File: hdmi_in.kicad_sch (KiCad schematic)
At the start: 46 parts, among them J3 HDMI_A, U1 M24C64-RMN6TP, U2 MS2109, U7 MT3520B, U8 MT3520B, Y1 24MHz 12pF

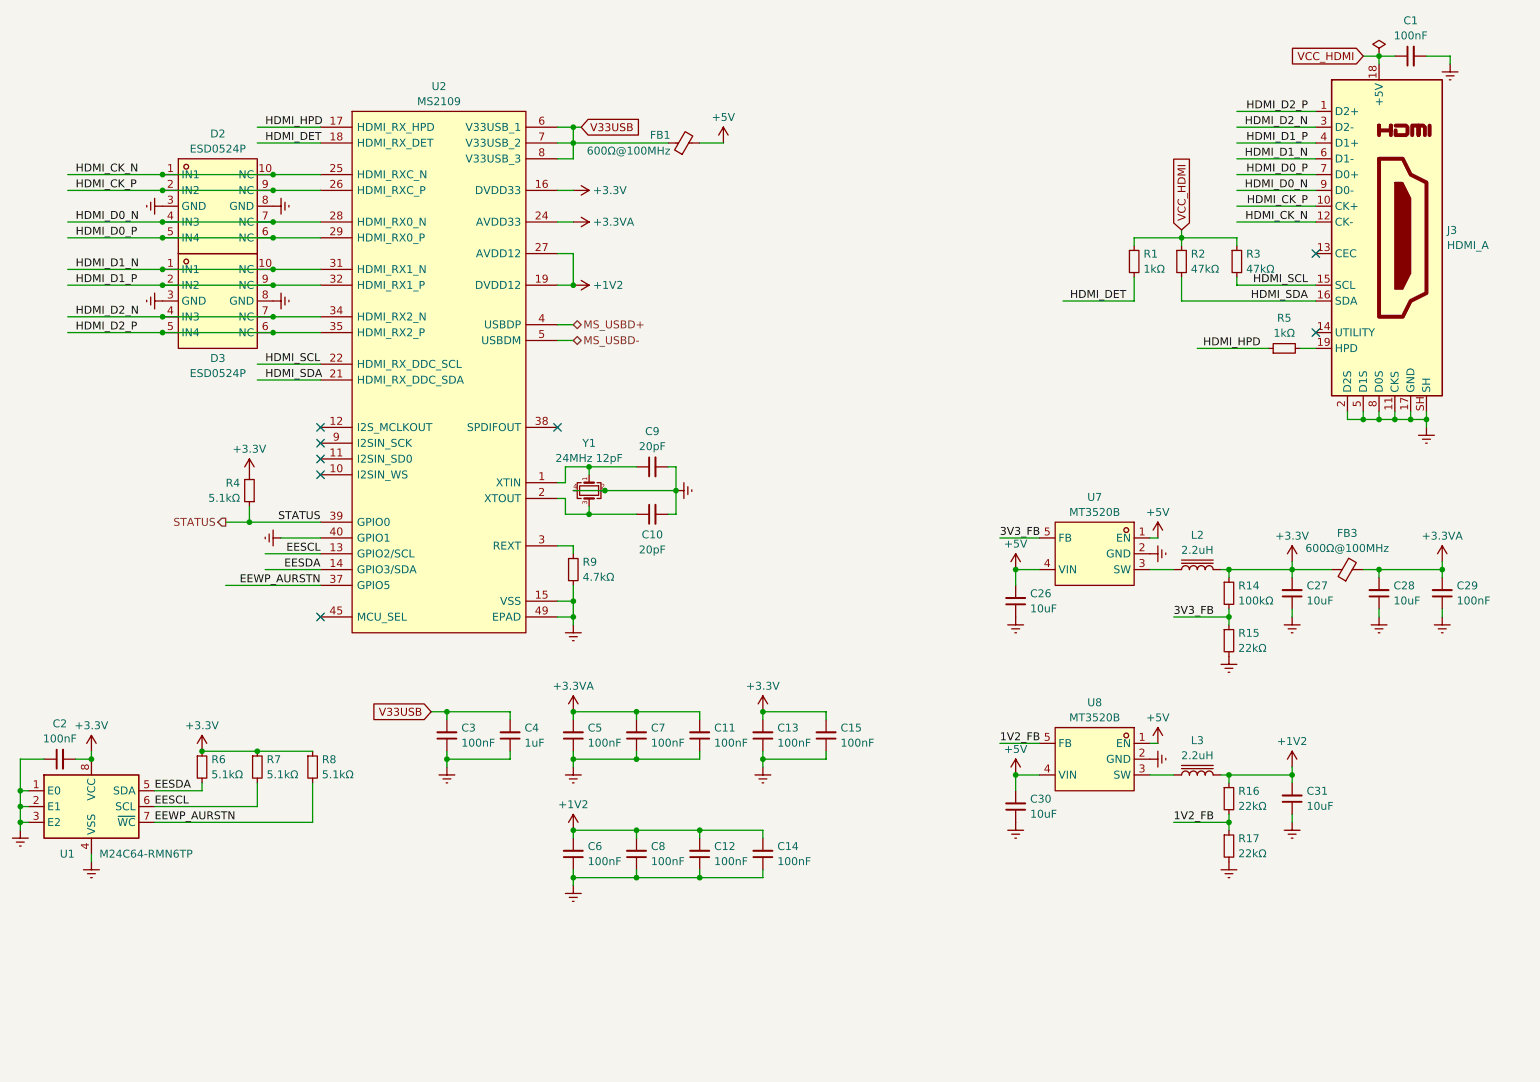
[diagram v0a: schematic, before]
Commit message: Update pcb & sch for T113 SOM
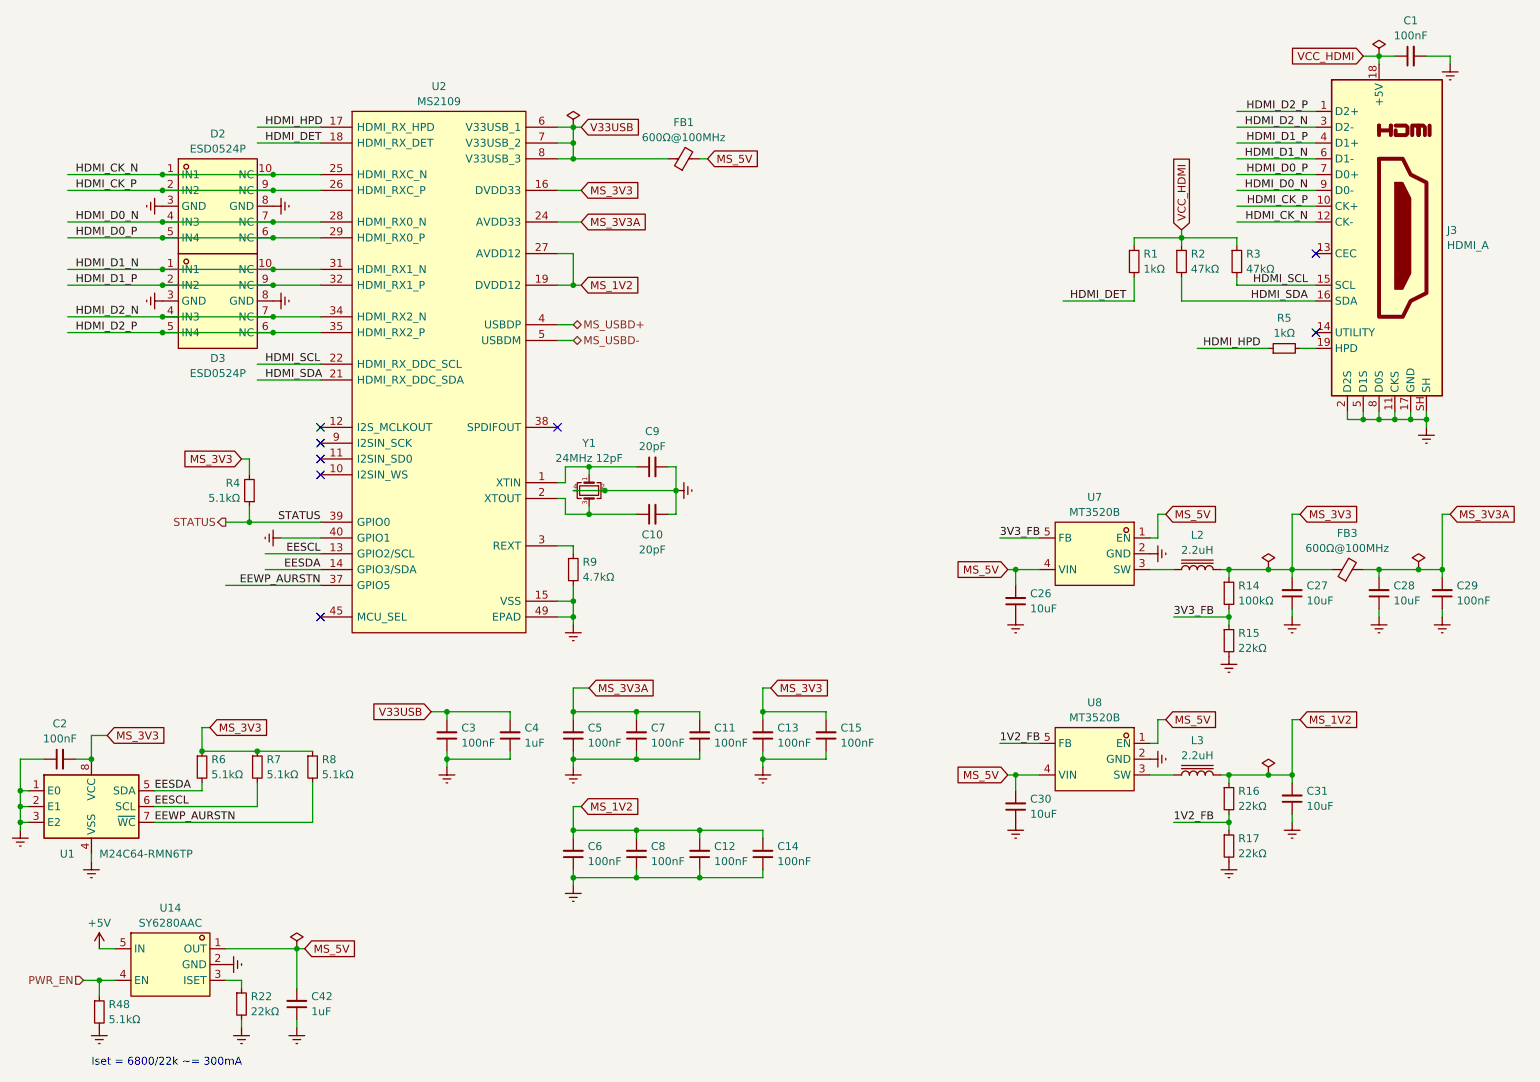
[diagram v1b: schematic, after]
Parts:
- added C42: 1uF, Capacitor_SMD:C_0402_1005Metric, symbol Device:C_Small
- added R22: 22kΩ, Resistor_SMD:R_0402_1005Metric, symbol Device:R_Small
- added R48: 5.1kΩ, Resistor_SMD:R_0402_1005Metric, symbol Device:R_Small
- added U14: SY6280AAC, Package_TO_SOT_SMD:SOT-23-5, symbol easyeda2kicad:SY6280AAC
- U7, U8: footprint easyeda2kicad:SOT-23-5_L3.0-W1.7-P0.95-LS2.8-BR -> Package_TO_SOT_SMD:SOT-23-5
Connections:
- net +5V: now also U14.5 (IN); no longer C26.2, C30.2, FB1.2, U7.1 (EN), U7.4 (VIN), U8.1 (EN), U8.4 (VIN)
- net Earth: now also C42.1, R22.2, R48.2, U14.2 (GND)
- net +1V2 renamed MS_1V2
- net +3.3V renamed MS_3V3
- net +3.3VA renamed MS_3V3A
- new net: R22.1, U14.3 (ISET)
- new net MS_5V: C26.2, C30.2, C42.2, FB1.2, U14.1 (OUT), U7.1 (EN), U7.4 (VIN), U8.1 (EN), U8.4 (VIN)
- new net PWR_EN: R48.1, U14.4 (EN)
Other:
- note added: "Iset = 6800/22k ~= 300mA"
- moved on the sheet: FB1

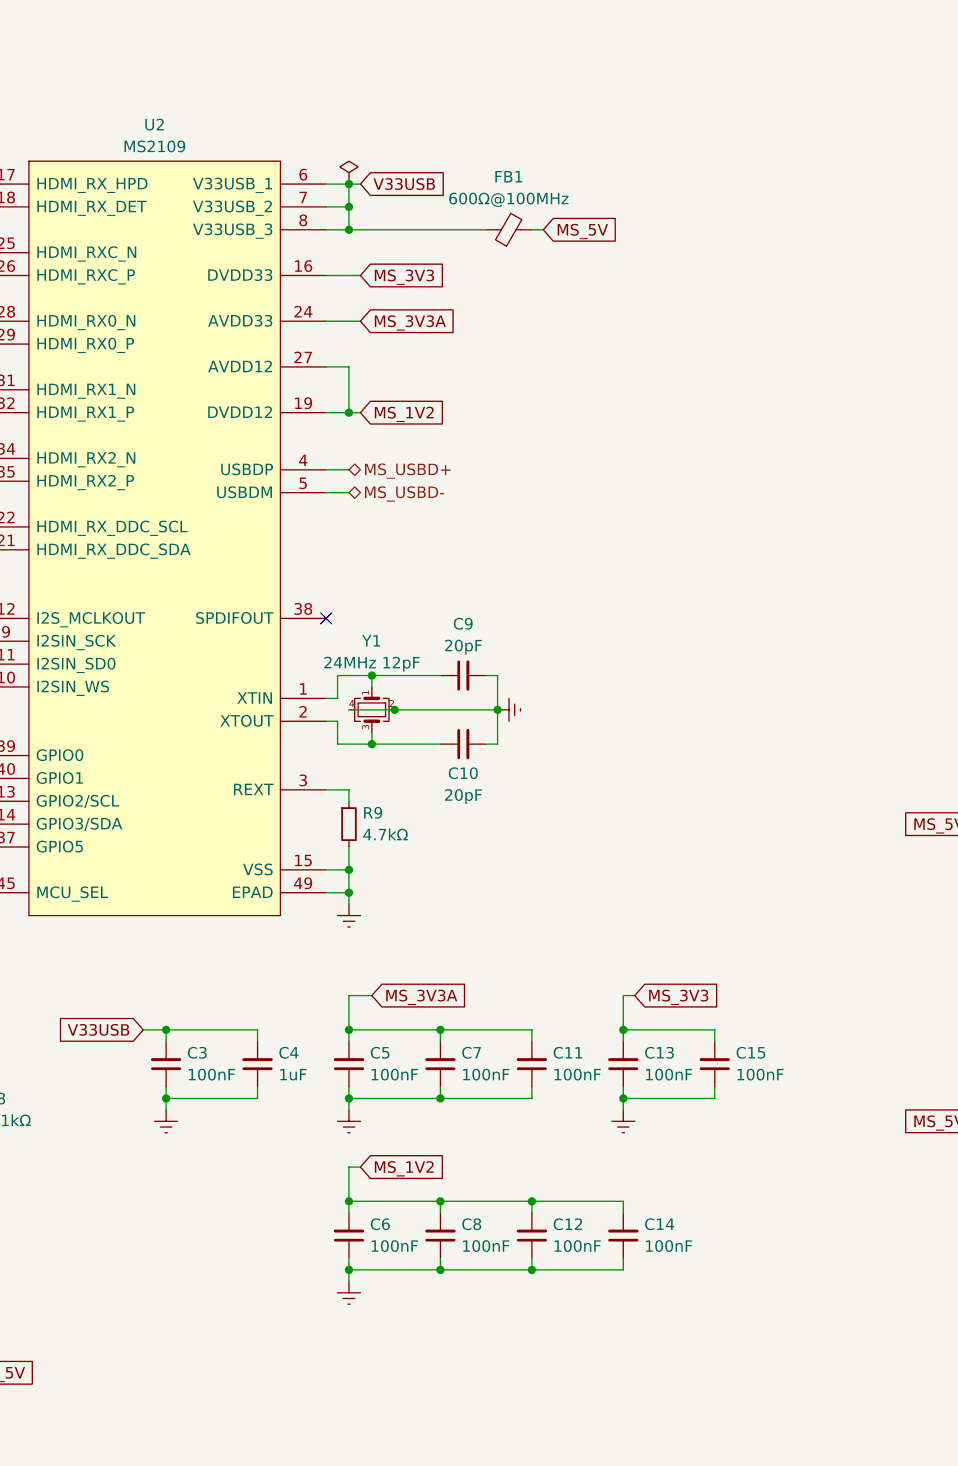
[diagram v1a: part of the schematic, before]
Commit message: Fix MS2109 symbol power pins, initial v1 release
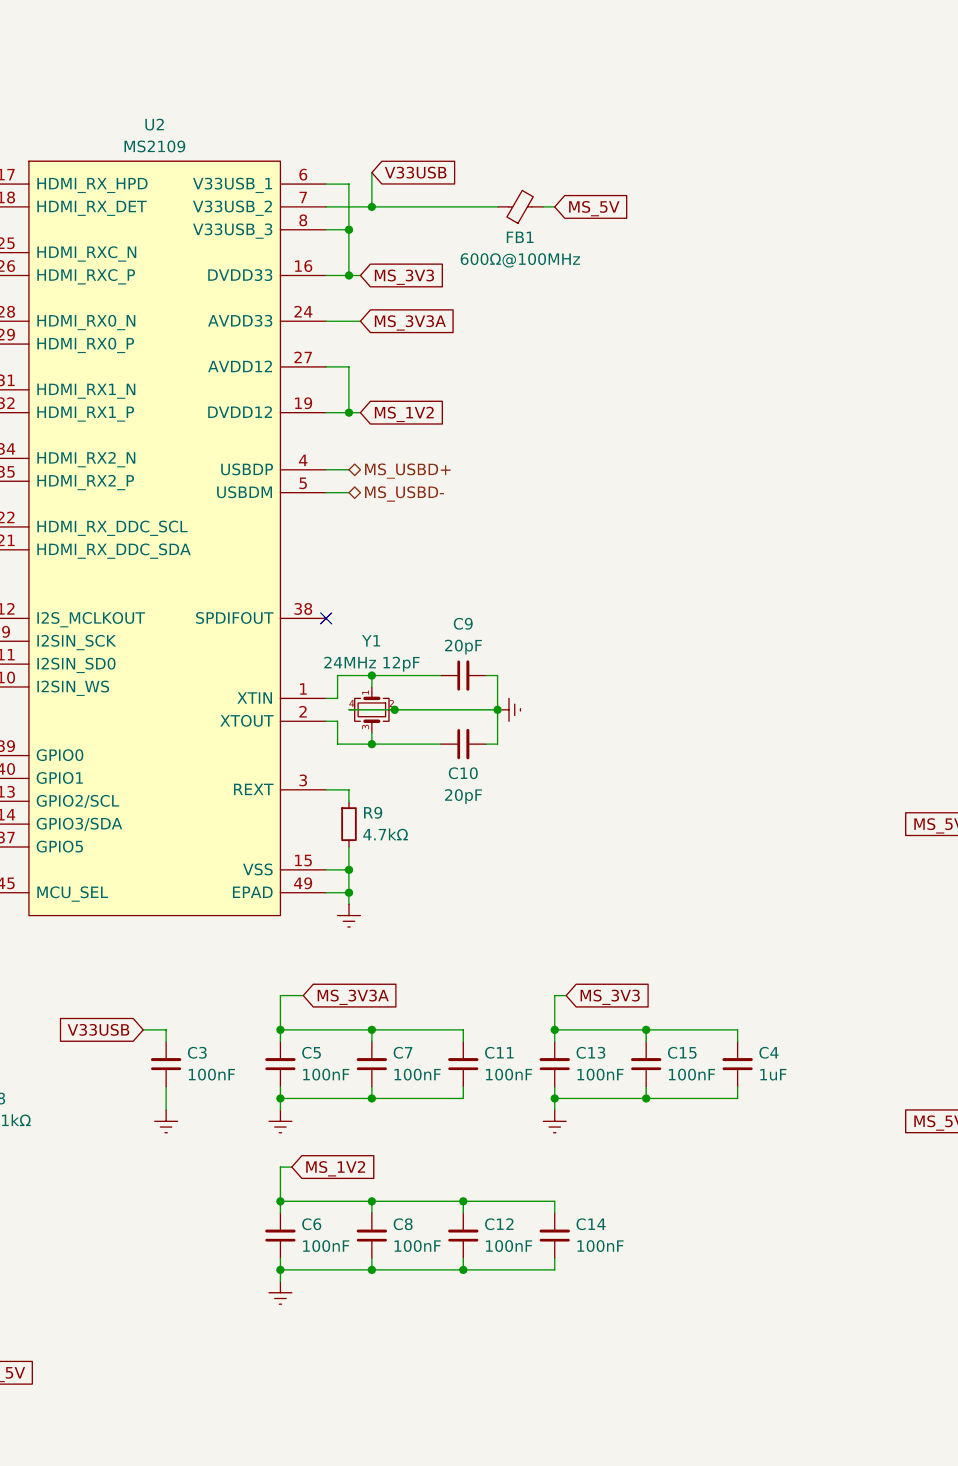
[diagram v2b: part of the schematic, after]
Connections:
- net Earth: no longer U2.44 (VSS)
- net MS_3V3: now also C4.2, U2.44 (DVDD33), U2.6 (V33USB_1), U2.8 (V33USB_3)
- net V33USB: no longer C4.2, U2.6 (V33USB_1), U2.8 (V33USB_3)
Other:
- moved on the sheet: C11, C12, C13, C14, C15, C4, C5, C6, C7, C8, FB1
